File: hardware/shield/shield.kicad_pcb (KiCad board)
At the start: 2 copper layers, 72.1 x 55.9 mm, 41 parts, among them J10 10118193-0001LF, U1 LM1117, Y1 12M

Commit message: New version of shield.
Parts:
- removed PA(X)11, PA11, PB(X)11, PB11, PC(X)11, PC11, PD(X)11, PD11: CON_HEADER_1X08-PTH, M1X8
- removed PROG(X)11, PROG11: CON_HEADER_1X06-PTH, M1X6
- removed PWR(X)11: CON_HEADER_1X03-PTH, M1X3
- removed R1, R2: 10k, 0603-RES
- removed U$2, U$3: TXS0101DBVR, SOT-23-6
- added U2: 4052, Housings_SOIC:SOIC-16_3.9x9.9mm_Pitch1.27mm, B.Cu at (155.7, 117.7)
- added U3: TXB0104, Housings_SOIC:SOIC-14_3.9x8.7mm_Pitch1.27mm, B.Cu at (140.5, 117.7)
- JP1: value 3v3Src1 -> ~
- JP2: value 3v3Src2 -> ~
- PA0, PB0, PC0, PD0, U1: moved to B.Cu
- PROG0: value PROG0 -> ~; moved to B.Cu
- PROG1: value PROG1 -> ~
- PWR0: value PWR0 -> ~; moved to B.Cu
- U$1: value CH340G -> ~
- moved PWR0 102.5 mm to (135.3, 85.9)
- moved PB0 92.9 mm to (135.3, 99.9), turned to 270 degrees
- moved PD1 91.3 mm to (144.2, 130.4)
- moved PB1 74.4 mm to (131.5, 99.9), turned to 270 degrees
- moved PD0 66.6 mm to (144.2, 126.6)
- moved PC0 65.5 mm to (163.3, 103.7), turned to 90 degrees
- moved PROG0 59.3 mm to (169.6, 126.6)
- moved PROG1 58.7 mm to (169.6, 130.4)
- moved C2 51.4 mm to (177.3, 83.4)
- moved PA0 51.2 mm to (154.4, 85.9)
- moved PA1 51.0 mm to (154.4, 82.1)
- moved C1 45.5 mm to (172.2, 83.4), turned to 0 degrees
- moved Y1 42.3 mm to (174.8, 87.2)
- moved PC1 39.2 mm to (167.1, 103.7), turned to 90 degrees
- moved U$1 32.2 mm to (177.3, 98.7), turned to 90 degrees
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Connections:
- net /5V renamed Vdd
- net /N$7 renamed /D-
- net /RXD renamed /RX
- net N$4 renamed D+
- C1 pad 1: /N$3 -> /XI
- C1 pad 2: /GND -> GND
- C2 pad 1: /N$5 -> /XO
- C2 pad 2: /GND -> GND
- C3 pad 1: /GND -> GND
- C4 pad 2: /GND -> GND
- C5 pad 2: /GND -> GND
- E1 pad 1: /TXD -> Net-(E1-Pad1)
- E1 pad 11: Net-(E1-Pad11) -> /3V3
- E1 pad 13: /GND -> GND
- E1 pad 14: /GND -> GND
- E1 pad 2: /N$1 -> Net-(E1-Pad2)
- E1 pad 21: /GND -> GND
- E1 pad 22: /GND -> GND
- E1 pad 26: /N$43 -> Net-(E1-Pad26)
- PROG0 pad 3: /TXD -> /TX
- PROG1 pad 3: /TXD -> /TX
- PWR0 pad 1: /GND -> GND
- PWR1 pad 1: /GND -> GND
- PWR2 pad 1: /GND -> GND
- PWR3 pad 1: /GND -> GND
- U$1 pad 1: /GND -> GND
- U$1 pad 2: /TXD -> /TX
- U$1 pad 7: /N$3 -> /XI
- U$1 pad 8: /N$5 -> /XO
- U1 pad 1: /GND -> GND
- Y1 pad 1: (no net) -> /XO
- Y1 pad 2: (no net) -> /XI
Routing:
- net /3V3: track 0.00 -> 93.0 mm
- net Vdd: track 0.00 -> 57.2 mm, vias 0 -> 4
- net Net-(E1-Pad2): track 0.00 -> 33.1 mm
- net Net-(E1-Pad24): track 0.00 -> 32.9 mm, vias 0 -> 2
- net Net-(E1-Pad1): track 0.00 -> 32.3 mm
- net Net-(E1-Pad25): track 0.00 -> 12.8 mm, vias 0 -> 2
- net GND: track 0.00 -> 3.85 mm, vias 0 -> 1
- net /N$40: track 0.00 -> 3.85 mm, vias 0 -> 1
- net /N$38: track 0.00 -> 3.85 mm, vias 0 -> 1
- net /N$37: track 0.00 -> 3.85 mm, vias 0 -> 1
- net /N$34: track 0.00 -> 3.85 mm, vias 0 -> 1
- net /N$33: track 0.00 -> 3.85 mm, vias 0 -> 1
- net /N$39: track 0.00 -> 3.85 mm, vias 0 -> 1
- net /N$36: track 0.00 -> 3.85 mm, vias 0 -> 1
- net /N$35: track 0.00 -> 3.85 mm, vias 0 -> 1
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- added copper zone on B.Cu, net GND
- removed copper zone on B.Cu, net (none)
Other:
- rule trace_min: 0.2 -> 0.25
- rule via_min_size: 0.4 -> 0.8

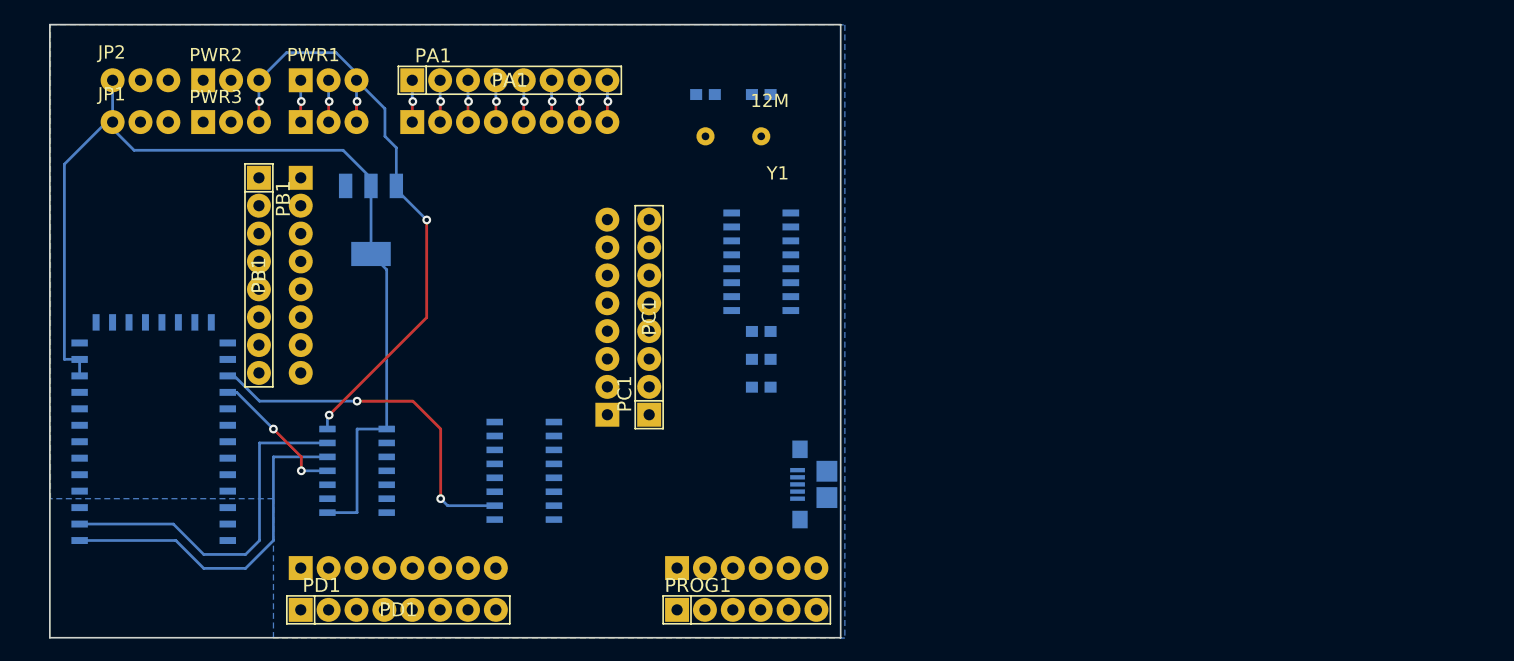
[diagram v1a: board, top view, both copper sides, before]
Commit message: Fully-routed; just the wrong size.
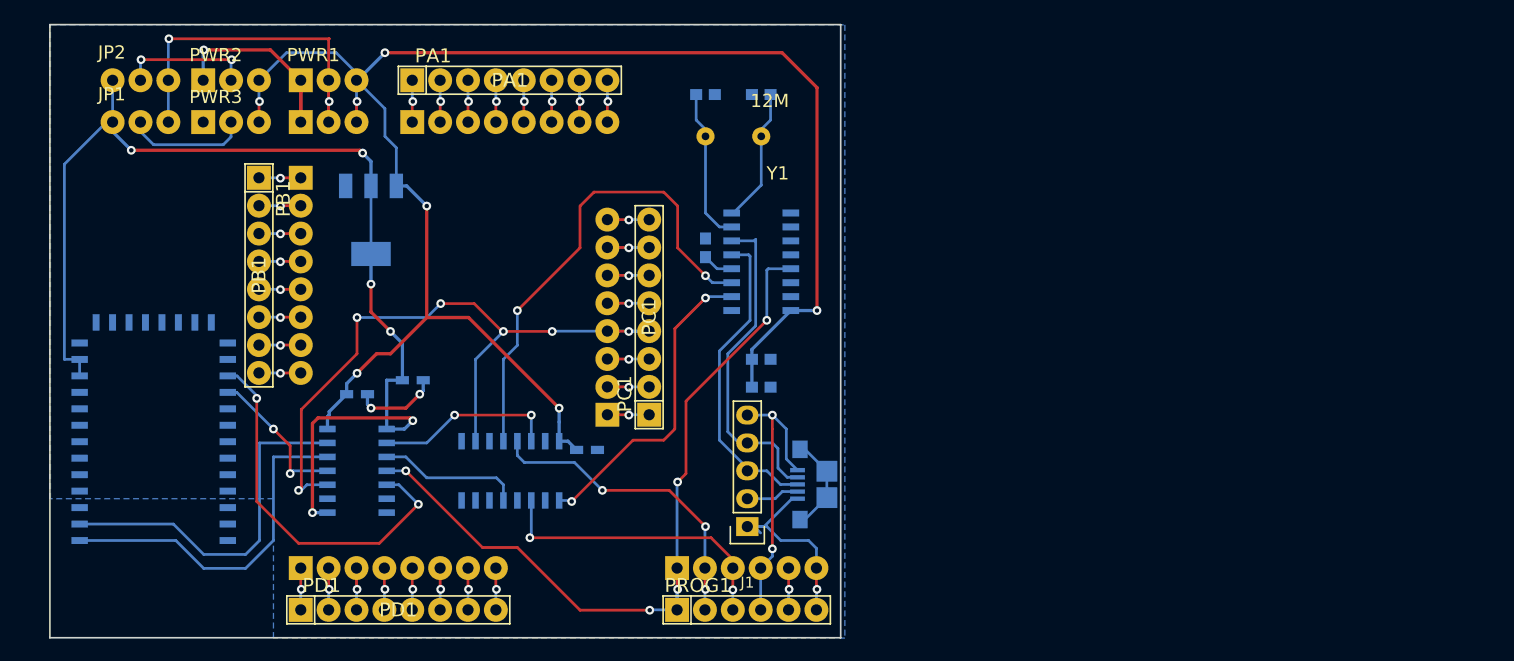
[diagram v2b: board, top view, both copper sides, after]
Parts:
- added C6: 0.1u, Capacitors_SMD:C_0603_HandSoldering, B.Cu at (161.4, 115.8)
- added C7: 0.1u, Capacitors_SMD:C_0603_HandSoldering, B.Cu at (145.5, 109.5)
- added C8: 0.1u, Capacitors_SMD:C_0603_HandSoldering, B.Cu at (140.5, 110.7)
- added J1: USBStandoff, Pin_Headers:Pin_Header_Straight_1x05, F.Cu at (176.0, 122.8)
- moved C3 9.16 mm to (172.2, 97.4), turned to 270 degrees
- moved U2 1.27 mm to (154.4, 117.7), turned to 90 degrees
- turned C4 to 0 degrees
- turned C5 to 0 degrees
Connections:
- U$1 pad 2: /TX -> /TXD-CH340G
- U$1 pad 3: /RX -> /RXD-CH340G
- U2 pad 1: /TX -> /TXD-CH340G
- U2 pad 10: Net-(E1-Pad24) -> /N$21
- U2 pad 12: /RX -> /RXD-CH340G
- U3 pad 10: Net-(U3-Pad10) -> /N$21
- U3 pad 5: Net-(U3-Pad5) -> Net-(E1-Pad24)
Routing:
- net Vdd: track 57.2 -> 155.2 mm, vias 4 -> 7
- net /DTR: track 0.00 -> 72.8 mm, vias 0 -> 5
- net /N$21: track 0.00 -> 63.9 mm, vias 0 -> 6
- net /RXD-CH340G: track 0.00 -> 44.3 mm, vias 0 -> 2
- net /D-: track 0.00 -> 30.4 mm
- net /N$2: track 3.85 -> 33.7 mm, vias 1 -> 2
- net /TXD-CH340G: track 0.00 -> 28.8 mm, vias 0 -> 2
- net /RX: track 0.00 -> 28.8 mm, vias 0 -> 3
- net D+: track 0.00 -> 28.7 mm
- net /TX: track 0.00 -> 27.4 mm, vias 0 -> 2
- net /N$6: track 0.00 -> 26.4 mm, vias 0 -> 2
- net GND: track 3.85 -> 28.2 mm, vias 1 -> 3
- net /N$41: track 0.00 -> 19.2 mm, vias 0 -> 1
- net Net-(U2-Pad14): track 0.00 -> 16.6 mm, vias 0 -> 2
- net /XI: track 0.00 -> 14.1 mm
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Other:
- net class Default: trace_width 0.25 -> 0.35
- net class Power added: clearance 0.3, trace_width 0.5, via_dia 0.8, via_drill 0.4

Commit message: Fully routed and with parts in reasonably OK spots.
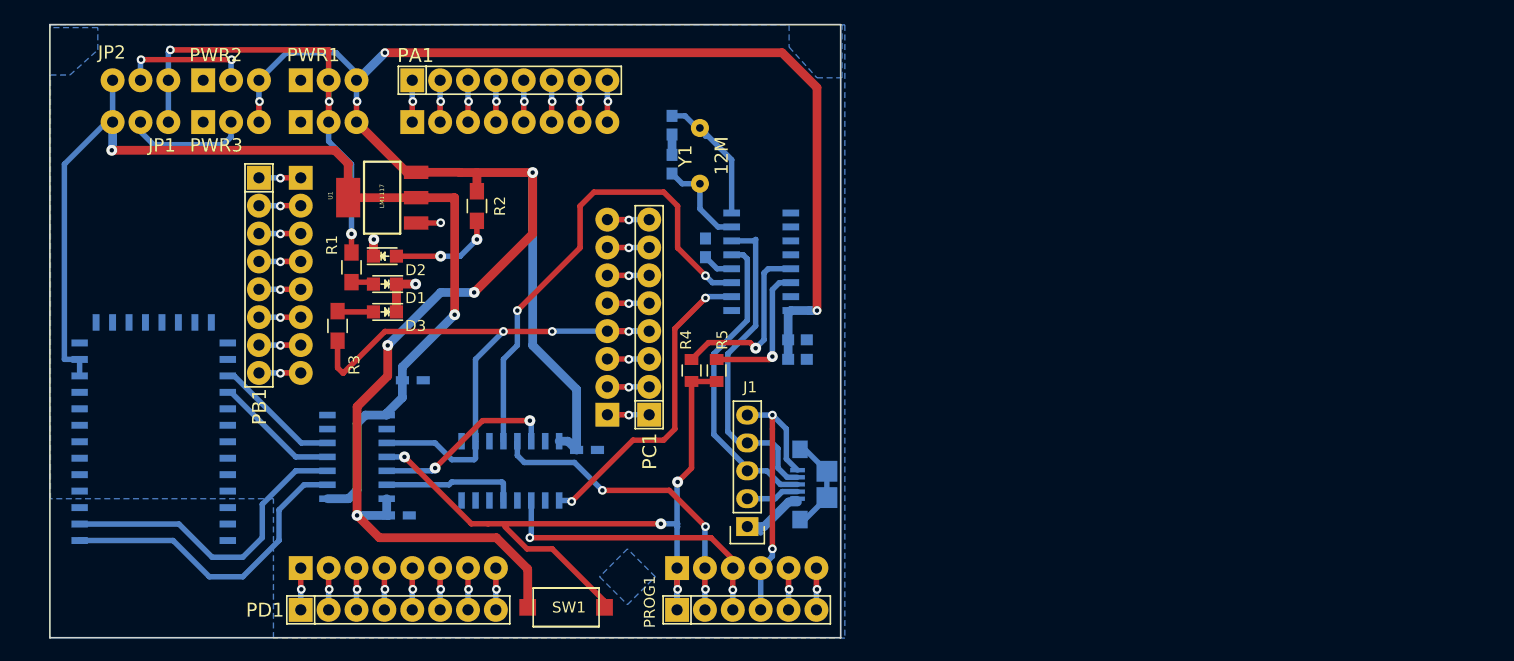
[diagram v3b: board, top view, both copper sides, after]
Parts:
- added D1: ORANGE, LEDs:LED_0805, F.Cu at (143.0, 100.7)
- added D2: RED, LEDs:LED_0805, F.Cu at (143.0, 98.2)
- added D3: BLUE, LEDs:LED_0805, F.Cu at (143.0, 103.3)
- added R1: 68, Resistors_SMD:R_0805_HandSoldering, F.Cu at (140.0, 99.2)
- added R2: 150, Resistors_SMD:R_0805_HandSoldering, F.Cu at (151.4, 93.6)
- added R3: 100, Resistors_SMD:R_0805_HandSoldering, F.Cu at (138.7, 104.5)
- added R4: DTR-RST, Capacitors_SMD:C_0805, F.Cu at (170.9, 108.6)
- added R5: RTS-RST, Capacitors_SMD:C_0805, F.Cu at (173.2, 108.6)
- added SW1: RESET, shield-pretty:NANO-SWITCH, F.Cu at (159.5, 129.9)
- J1: value USBStandoff -> ~
- PA0: value PA0 -> ~
- PA1: value PA1 -> ~
- PB0: value PB0 -> ~
- PB1: value PB1 -> ~
- PC0: value PC0 -> ~
- PC1: value PC1 -> ~
- PD0: value PD0 -> ~
- PD1: value PD1 -> ~
- PWR1: value PWR1 -> ~
- PWR2: value PWR2 -> ~
- PWR3: value PWR3 -> ~
- U1: moved to F.Cu
- U2: value 4052 -> 74LV4052
- moved C8 11.7 mm to (144.3, 121.8)
- moved C2 8.59 mm to (169.2, 86.2), turned to 270 degrees
- moved C1 7.04 mm to (169.2, 89.8), turned to 90 degrees
- moved C5 4.17 mm to (180.6, 107.6)
- moved C4 3.75 mm to (180.6, 105.8)
- moved Y1 3.53 mm to (171.7, 89.0), turned to 270 degrees
- moved U1 2.27 mm to (142.7, 92.8), turned to 90 degrees
- moved U3 1.27 mm to (140.5, 116.5), turned to 0 degrees
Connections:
- net Net-(E1-Pad24) renamed /CONN-BT
- E1 pad $7: Net-(E1-Pad$7) -> (no net)
- E1 pad 10: Net-(E1-Pad10) -> (no net)
- E1 pad 15: Net-(E1-Pad15) -> (no net)
- E1 pad 16: Net-(E1-Pad16) -> (no net)
- E1 pad 17: Net-(E1-Pad17) -> (no net)
- E1 pad 18: Net-(E1-Pad18) -> (no net)
- E1 pad 19: Net-(E1-Pad19) -> (no net)
- E1 pad 20: Net-(E1-Pad20) -> (no net)
- E1 pad 23: Net-(E1-Pad23) -> (no net)
- E1 pad 25: Net-(E1-Pad25) -> /DTR-BT
- E1 pad 26: Net-(E1-Pad26) -> (no net)
- E1 pad 27: Net-(E1-Pad27) -> (no net)
- E1 pad 28: Net-(E1-Pad28) -> (no net)
- E1 pad 29: Net-(E1-Pad29) -> (no net)
- E1 pad 3: Net-(E1-Pad3) -> (no net)
- E1 pad 30: Net-(E1-Pad30) -> (no net)
- E1 pad 31: Net-(E1-Pad31) -> (no net)
- E1 pad 32: Net-(E1-Pad32) -> (no net)
- E1 pad 33: Net-(E1-Pad33) -> (no net)
- E1 pad 34: Net-(E1-Pad34) -> (no net)
- E1 pad 4: Net-(E1-Pad4) -> (no net)
- E1 pad 5: Net-(E1-Pad5) -> (no net)
- E1 pad 6: Net-(E1-Pad6) -> (no net)
- E1 pad 8: Net-(E1-Pad8) -> (no net)
- E1 pad 9: Net-(E1-Pad9) -> (no net)
- J1 pad 1: /N$41 -> GND
- J10 pad GND: /N$41 -> GND
- PROG0 pad 6: /N$41 -> GND
- PROG1 pad 6: /N$41 -> GND
- U$1 pad 10: Net-(U$1-Pad10) -> (no net)
- U$1 pad 11: Net-(U$1-Pad11) -> (no net)
- U$1 pad 12: Net-(U$1-Pad12) -> (no net)
- U$1 pad 13: /DTR -> /DTR-USB
- U$1 pad 15: Net-(U$1-Pad15) -> (no net)
- U$1 pad 9: Net-(U$1-Pad9) -> (no net)
- U2 pad 11: Net-(U2-Pad11) -> (no net)
- U2 pad 15: Net-(U2-Pad15) -> (no net)
- U2 pad 2: Net-(U2-Pad2) -> (no net)
- U2 pad 4: Net-(U2-Pad4) -> (no net)
- U3 pad 11: Net-(E1-Pad25) -> /DTR
- U3 pad 12: Net-(E1-Pad1) -> Net-(U2-Pad14)
- U3 pad 13: Net-(E1-Pad2) -> Net-(U2-Pad5)
- U3 pad 2: Net-(U2-Pad14) -> Net-(E1-Pad1)
- U3 pad 3: Net-(U2-Pad5) -> Net-(E1-Pad2)
- U3 pad 4: /DTR -> /DTR-BT
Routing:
- net Vdd: track 155.2 -> 205.4 mm, vias 7 -> 8
- net /CONN-BT: track 35.0 -> 11.6 mm, vias 2 -> 0
- net /N$41: track 19.2 -> 0.00 mm, vias 1 -> 0
- net /DTR-USB: track 0.00 -> 16.5 mm, vias 0 -> 1
- net Net-(E1-Pad25): track 13.7 -> 0.00 mm, vias 2 -> 0
- net Net-(R5-Pad1): track 0.00 -> 13.2 mm, vias 0 -> 1
- net /DTR-BT: track 0.00 -> 11.5 mm
- net /N$2: track 33.7 -> 44.3 mm, vias 2 -> 3
- net Net-(D2-Pad2): track 0.00 -> 9.66 mm, vias 0 -> 2
- net GND: track 28.2 -> 21.1 mm, vias 3 -> 4
- net /XI: track 14.1 -> 8.79 mm
- net Net-(E1-Pad2): track 33.1 -> 28.9 mm
- net /N$21: track 63.9 -> 59.9 mm, vias 6 -> 3
- net Net-(D3-Pad2): track 0.00 -> 3.30 mm
- net Net-(E1-Pad1): track 32.3 -> 29.1 mm
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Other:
- net class Default: trace_width 0.35 -> 0.5; via_dia 0.8 -> 1
- net class Power: trace_width 0.5 -> 0.8; via_dia 0.8 -> 1

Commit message: Fully working; switched to USB MINI B.
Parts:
- removed J1: ~, Pin_Headers:Pin_Header_Straight_1x05
- added R6: 3V3USB, Capacitors_SMD:C_0805, F.Cu at (156.1, 94.4)
- C1, C2, C3, C5: footprint 0603-CAP -> Capacitors_SMD:C_0805_HandSoldering
- C4: footprint 0603-CAP -> Capacitors_THT:C_Radial_D5_L6_P2.5; moved to F.Cu
- C6, C7, C8: footprint Capacitors_SMD:C_0603_HandSoldering -> Capacitors_SMD:C_0805_HandSoldering
- E1: footprint 26.9X13X2.2_BOARD -> shield:JNHUAMAO_26.9X13X2.2_BOARD
- J10: value 10118193-0001LF -> USB_OTG; footprint 10118193-0001LF -> shield-pretty:USB_Mini-B
- JP1, JP2: footprint 1X03 -> Pin_Headers:Pin_Header_Straight_1x03
- PWR1, PWR2, PWR3: footprint M1X3 -> shield:DP_DEVICES.V6_M1X3
- U$1: footprint SOIC16 -> shield:CH340G_SOIC16
- Y1: footprint HC49US -> Crystals:Crystal_HC49-U_Vertical
- moved C6 9.88 mm to (158.4, 106.4), turned to 90 degrees
- moved PROG1 7.59 mm to (169.7, 122.8)
- moved PD1 7.34 mm to (144.3, 123.1)
- moved J10 5.30 mm to (179.8, 114.9), turned to 180 degrees
- moved U2 5.09 mm to (154.2, 112.6)
- moved C7 4.83 mm to (145.3, 104.6)
- moved U3 4.35 mm to (141.0, 112.1)
- moved C8 3.99 mm to (144.9, 117.9)
- moved SW1 3.82 mm to (159.3, 126.1)
- moved C2 3.70 mm to (168.1, 82.7), turned to 90 degrees
- moved E1 3.38 mm to (120.8, 121.3)
- moved Y1 2.67 mm to (171.8, 86.4)
- moved C1 2.27 mm to (168.1, 87.8)
- moved C5 2.26 mm to (182.0, 105.8), turned to 270 degrees
- moved C4 1.31 mm to (180.0, 104.6), turned to 270 degrees
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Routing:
- net Vdd: track 205.4 -> 180.7 mm
- net /N$8: track 2.82 -> 25.0 mm, vias 0 -> 1
- net /TX: track 27.4 -> 39.5 mm, vias 2 -> 3
- net GND: track 21.1 -> 9.85 mm, vias 4 -> 3
- net /RX: track 28.8 -> 39.5 mm
- net Net-(J10-PadSHIE): track 8.96 -> 0.00 mm
- net /D-: track 30.4 -> 24.2 mm
- net /N$21: track 59.9 -> 54.9 mm, vias 3 -> 4
- net Net-(J1-Pad2): track 4.85 -> 0.00 mm
- net D+: track 28.6 -> 24.1 mm
- net /RXD-CH340G: track 44.3 -> 39.8 mm
- net /3V3: track 103.9 -> 107.8 mm
- net /CONN-BT: track 11.6 -> 15.4 mm
- net /XI: track 8.79 -> 12.3 mm
- net /DTR-BT: track 11.5 -> 14.8 mm
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- added copper zone on F.Cu, net GND
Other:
- board size 72.1 x 55.9 mm -> 74.5 x 51.6 mm
- net class TINY added: clearance 0.2, trace_width 0.35, via_dia 1, via_drill 0.4
